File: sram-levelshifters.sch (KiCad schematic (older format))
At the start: 5 parts, among them U1 74HC04, U7 ISSI61WV5128BL, U8 ISSI61WV5128BL

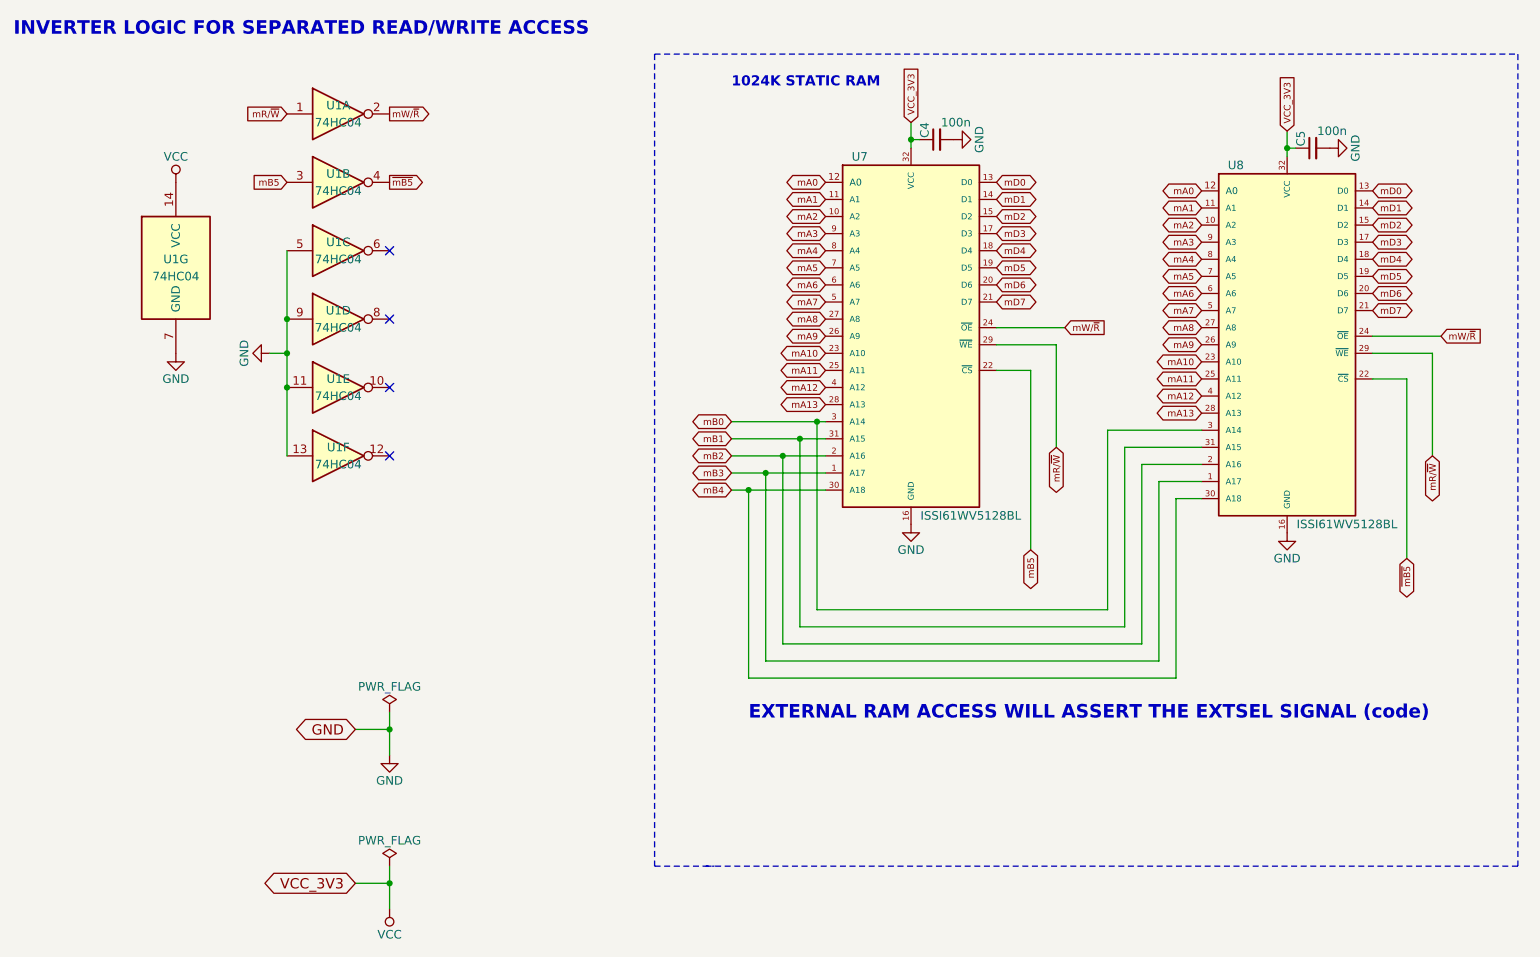
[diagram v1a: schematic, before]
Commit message: Upgraded to a dual chip select for external SRAM. In this case up to 1536k can be addressable
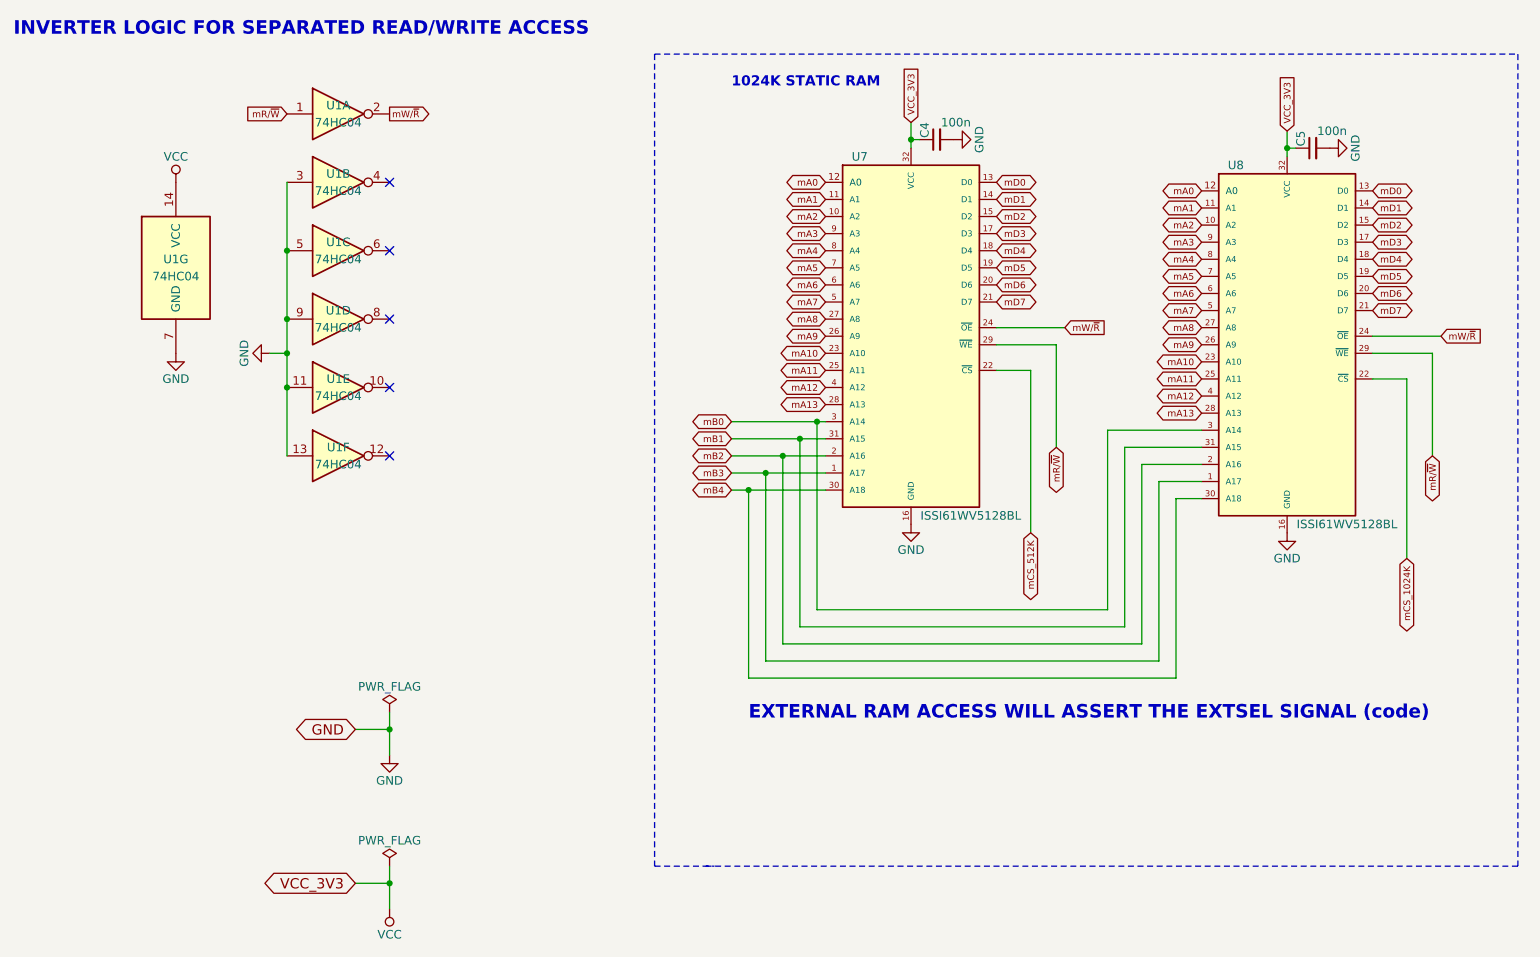
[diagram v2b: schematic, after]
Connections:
- net GND: now also U1.3
- net mB5 renamed mCS_512K
- net mCS_512K: no longer U1.3
- net ~mB5: no longer names the net of U1.4
- net ~mB5: no longer U8.22 (~CS)
- new net mCS_1024K: U8.22 (~CS)
- no-connect marks 4 -> 5
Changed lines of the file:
@@
 Wire Wire Line
 	7050 3300 7250 3300
-Wire Wire Line
-	7250 3300 7250 4350
-Text GLabel 7250 4350 3    39   BiDi ~ 0
-mB5
+Text GLabel 7250 4250 3    39   BiDi ~ 0
+mCS_512K
 Text Notes 5600 5350 0    79   ~ 16
 EXTERNAL RAM ACCESS WILL ASSERT THE EXTSEL SIGNAL (code)
@@
 Wire Wire Line
 	9450 3350 9450 4400
-Text GLabel 9450 4400 3    39   BiDi ~ 0
-~mB5
 Wire Wire Line
 	5500 3600 6050 3600
@@
 	1    0    0    -1
 $EndComp
-Text GLabel 2900 2200 0    39   Input ~ 0
-mB5
-Text GLabel 3500 2200 2    39   Output ~ 0
-~mB5
 Text Notes 1300 1350 0    79   ~ 16
 INVERTER LOGIC FOR SEPARATED READ/WRITE ACCESS
@@
 $EndComp
 Wire Wire Line
-	2900 2600 2900 3800
+	2900 2200 2900 3800
 Connection ~ 2900 3000
 Connection ~ 2900 3400
@@
 	2800 3200 2900 3200
 Connection ~ 2900 3200
+Connection ~ 2900 2600
+NoConn ~ 3500 2200
+Wire Wire Line
+	7250 3300 7250 4250
+Text GLabel 9450 4400 3    39   BiDi ~ 0
+mCS_1024K
 $EndSCHEMATC

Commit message: Added nOE and nWE from the GPIOs
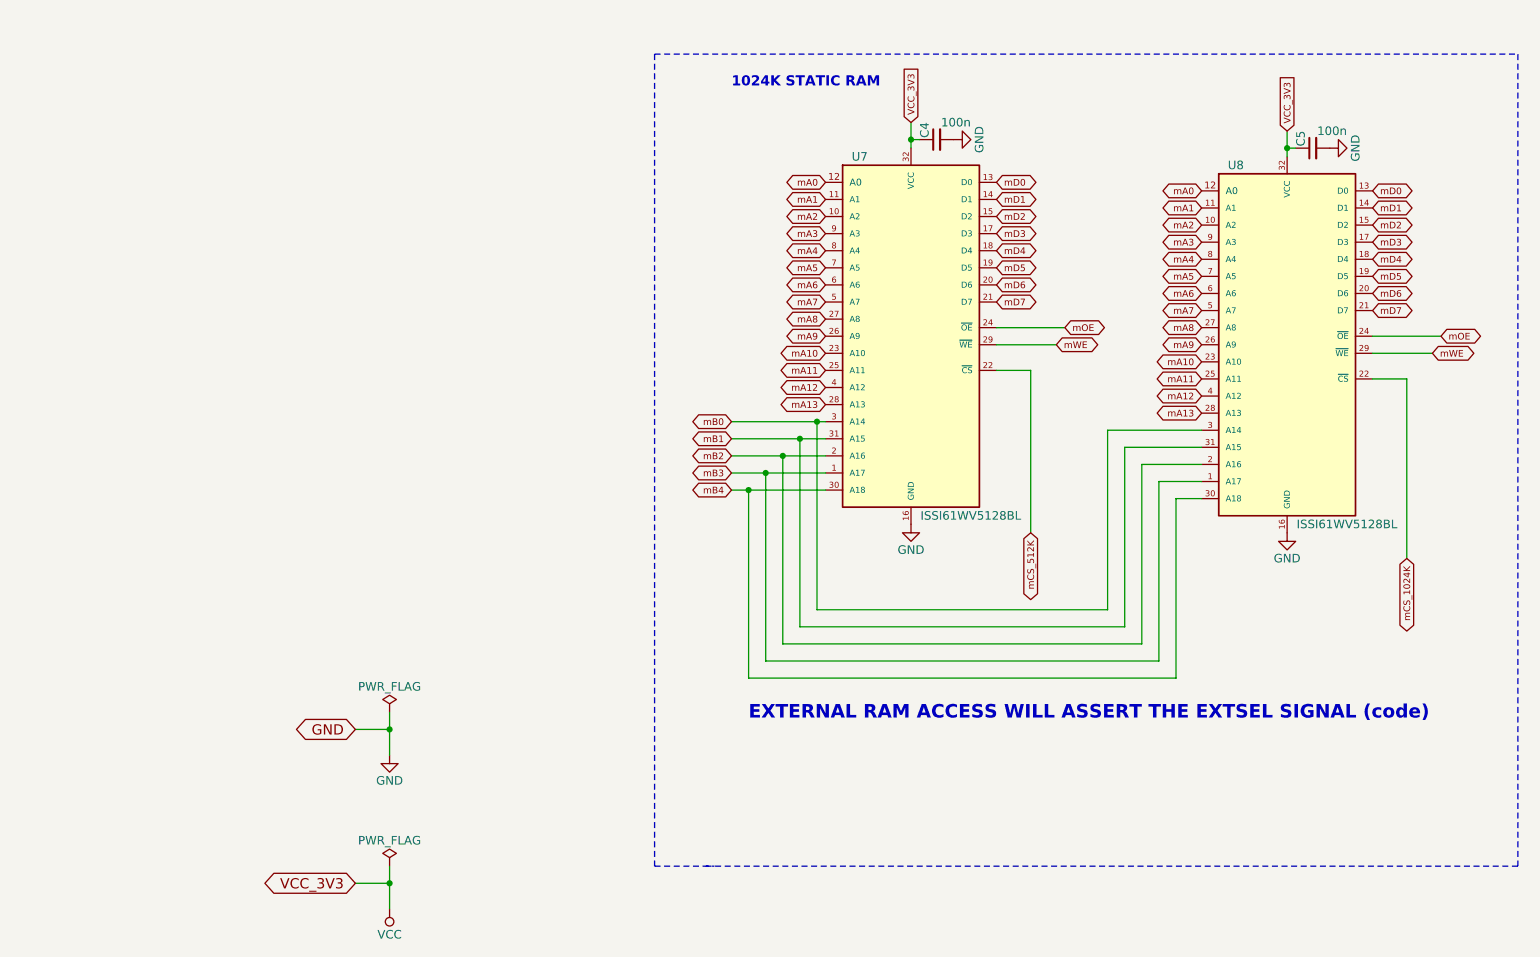
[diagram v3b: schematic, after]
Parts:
- removed U1: 74HC04, RetroBitLab:PSOP14-5x7.40-1.27, symbol 74HC04
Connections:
- net mR/~W renamed mWE
- net mW/~R renamed mOE
- no-connect marks 5 -> 0
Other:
- note removed: "INVERTER LOGIC FOR SEPARATED READ/WRITE ACCESS"
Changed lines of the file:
@@
 Text GLabel 6550 1850 1    39   Input ~ 0
 VCC_3V3
-Text GLabel 7400 3750 3    39   BiDi ~ 0
-mR/~W
 Wire Wire Line
 	7050 3150 7400 3150
-Wire Wire Line
-	7400 3150 7400 3750
 Wire Wire Line
 	6550 1850 6550 2000
@@
 Text GLabel 8750 1900 1    39   Input ~ 0
 VCC_3V3
-Text GLabel 9600 3800 3    39   BiDi ~ 0
-mR/~W
 Wire Wire Line
 	9250 3200 9600 3200
-Wire Wire Line
-	9600 3200 9600 3800
 Wire Wire Line
 	8750 1900 8750 2050
@@
 Wire Wire Line
 	7450 3050 7050 3050
-$Comp
-L 74HC04 U1
-U 1 1 5CC43BF6
-P 3200 1800
-F 0 "U1" H 3200 1850 50  0000 C CNN
-F 1 "74HC04" H 3200 1750 50  0000 C CNN
-F 2 "RetroBitLab:PSOP14-5x7.40-1.27" H 3200 1800 50  0001 C CNN
-F 3 "" H 3200 1800 50  0001 C CNN
-	1    3200 1800
-	1    0    0    -1
-$EndComp
-Text GLabel 2900 1800 0    39   Input ~ 0
-mR/~W
-Text GLabel 3500 1800 2    39   Output ~ 0
-mW/~R
-Text GLabel 7450 3050 2    39   Input ~ 0
-mW/~R
-Text GLabel 9650 3100 2    39   Input ~ 0
-mW/~R
-$Comp
-L 74HC04 U1
-U 2 1 5CC43DF2
-P 3200 2200
-F 0 "U1" H 3200 2250 50  0000 C CNN
-F 1 "74HC04" H 3200 2150 50  0000 C CNN
-F 2 "RetroBitLab:PSOP14-5x7.40-1.27" H 3200 2200 50  0001 C CNN
-F 3 "" H 3200 2200 50  0001 C CNN
-	2    3200 2200
-	1    0    0    -1
-$EndComp
-Text Notes 1300 1350 0    79   ~ 16
-INVERTER LOGIC FOR SEPARATED READ/WRITE ACCESS
-$Comp
-L 74HC04 U1
-U 3 1 5CC43E84
-P 3200 2600
-F 0 "U1" H 3200 2650 50  0000 C CNN
-F 1 "74HC04" H 3200 2550 50  0000 C CNN
-F 2 "RetroBitLab:PSOP14-5x7.40-1.27" H 3200 2600 50  0001 C CNN
-F 3 "" H 3200 2600 50  0001 C CNN
-	3    3200 2600
-	1    0    0    -1
-$EndComp
-$Comp
-L 74HC04 U1
-U 4 1 5CC43EC9
-P 3200 3000
-F 0 "U1" H 3200 3050 50  0000 C CNN
-F 1 "74HC04" H 3200 2950 50  0000 C CNN
-F 2 "RetroBitLab:PSOP14-5x7.40-1.27" H 3200 3000 50  0001 C CNN
-F 3 "" H 3200 3000 50  0001 C CNN
-	4    3200 3000
-	1    0    0    -1
-$EndComp
-$Comp
-L 74HC04 U1
-U 5 1 5CC43F00
-P 3200 3400
-F 0 "U1" H 3200 3450 50  0000 C CNN
-F 1 "74HC04" H 3200 3350 50  0000 C CNN
-F 2 "RetroBitLab:PSOP14-5x7.40-1.27" H 3200 3400 50  0001 C CNN
-F 3 "" H 3200 3400 50  0001 C CNN
-	5    3200 3400
-	1    0    0    -1
-$EndComp
-$Comp
-L 74HC04 U1
-U 6 1 5CC43FFF
-P 3200 3800
-F 0 "U1" H 3200 3850 50  0000 C CNN
-F 1 "74HC04" H 3200 3750 50  0000 C CNN
-F 2 "RetroBitLab:PSOP14-5x7.40-1.27" H 3200 3800 50  0001 C CNN
-F 3 "" H 3200 3800 50  0001 C CNN
-	6    3200 3800
-	1    0    0    -1
-$EndComp
-$Comp
-L 74HC04 U1
-U 7 1 5CC4404C
-P 2250 2700
-F 0 "U1" H 2250 2750 50  0000 C CNN
-F 1 "74HC04" H 2250 2650 50  0000 C CNN
-F 2 "RetroBitLab:PSOP14-5x7.40-1.27" H 2250 2700 50  0001 C CNN
-F 3 "" H 2250 2700 50  0001 C CNN
-	7    2250 2700
-	1    0    0    -1
-$EndComp
-$Comp
-L GND #PWR017
-U 1 1 5CC440E8
-P 2250 3200
-F 0 "#PWR017" H 2250 2950 50  0001 C CNN
-F 1 "GND" H 2250 3050 50  0000 C CNN
-F 2 "" H 2250 3200 50  0001 C CNN
-F 3 "" H 2250 3200 50  0001 C CNN
-	1    2250 3200
-	1    0    0    -1
-$EndComp
-$Comp
-L VCC #PWR018
-U 1 1 5CC44114
-P 2250 2200
-F 0 "#PWR018" H 2250 2050 50  0001 C CNN
-F 1 "VCC" H 2250 2350 50  0000 C CNN
-F 2 "" H 2250 2200 50  0001 C CNN
-F 3 "" H 2250 2200 50  0001 C CNN
-	1    2250 2200
-	1    0    0    -1
-$EndComp
-Wire Wire Line
-	2900 2200 2900 3800
-Connection ~ 2900 3000
-Connection ~ 2900 3400
-NoConn ~ 3500 2600
-NoConn ~ 3500 3000
-NoConn ~ 3500 3400
-NoConn ~ 3500 3800
-$Comp
-L GND #PWR019
-U 1 1 5CC44296
-P 2800 3200
-F 0 "#PWR019" H 2800 2950 50  0001 C CNN
-F 1 "GND" H 2800 3050 50  0000 C CNN
-F 2 "" H 2800 3200 50  0001 C CNN
-F 3 "" H 2800 3200 50  0001 C CNN
-	1    2800 3200
-	0    1    1    0
-$EndComp
-Wire Wire Line
-	2800 3200 2900 3200
-Connection ~ 2900 3200
-Connection ~ 2900 2600
-NoConn ~ 3500 2200
 Wire Wire Line
 	7250 3300 7250 4250
 Text GLabel 9450 4400 3    39   BiDi ~ 0
 mCS_1024K
+Text GLabel 9650 3100 2    39   BiDi ~ 0
+mOE
+Text GLabel 9600 3200 2    39   BiDi ~ 0
+mWE
+Text GLabel 7450 3050 2    39   BiDi ~ 0
+mOE
+Text GLabel 7400 3150 2    39   BiDi ~ 0
+mWE
 $EndSCHEMATC

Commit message: New layout and design
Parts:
- removed C5: 100n, Capacitors_SMD:C_1206_HandSoldering, symbol C_Small
- removed U8: ISSI61WV5128BL, RetroBitLab:SOP-32L-20.5x11.30-1.27mm, symbol ISSI61WV5128BL
- added C3: 100n, Capacitors_SMD:C_1206_HandSoldering, symbol C_Small
- added U2: ISSI61WV5128BL, RetroBitLab:SOP-32L-20.5x11.30-1.27mm, symbol ISSI61WV5128BL
- renumbered C4 to C2, U7 to U1
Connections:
- net GND: now also C3.2, U2.16 (GND)
- net VCC: now also C3.1, U2.32 (VCC)
- net mA0 renamed FSMC_A0
- net FSMC_A0: now also U2.12 (A0)
- net mA1 renamed FSMC_A1
- net FSMC_A1: now also U2.11 (A1)
- net mA10 renamed FSMC_A10
- net FSMC_A10: now also U2.23 (A10)
- net mA11 renamed FSMC_A11
- net FSMC_A11: now also U2.25 (A11)
- net mA12 renamed FSMC_A12
- net FSMC_A12: now also U2.4 (A12)
- net mA13 renamed FSMC_A13
- net FSMC_A13: now also U2.28 (A13)
- net mA2 renamed FSMC_A2
- net FSMC_A2: now also U2.10 (A2)
- net mA3 renamed FSMC_A3
- net FSMC_A3: now also U2.9 (A3)
- net mA4 renamed FSMC_A4
- net FSMC_A4: now also U2.8 (A4)
- net mA5 renamed FSMC_A5
- net FSMC_A5: now also U2.7 (A5)
- net mA6 renamed FSMC_A6
- net FSMC_A6: now also U2.6 (A6)
- net mA7 renamed FSMC_A7
- net FSMC_A7: now also U2.5 (A7)
- net mA8 renamed FSMC_A8
- net FSMC_A8: now also U2.27 (A8)
- net mA9 renamed FSMC_A9
- net FSMC_A9: now also U2.26 (A9)
- net mB0 renamed FSMC_A14
- net FSMC_A14: now also U2.3 (A14)
- net mB1 renamed FSMC_A15
- net FSMC_A15: now also U2.31 (A15)
- net mB2 renamed FSMC_A16
- net FSMC_A16: now also U2.2 (A16)
- net mB3 renamed FSMC_A17
- net FSMC_A17: now also U2.1 (A17)
- net mB4 renamed FSMC_A18
- net FSMC_A18: now also U2.30 (A18)
- net mCS_512K renamed FSMC_NE1
- net mD0 renamed FSMC_D0
- net FSMC_D0: now also U2.13 (D0)
- net mD1 renamed FSMC_D1
- net FSMC_D1: now also U2.14 (D1)
- net mD2 renamed FSMC_D2
- net FSMC_D2: now also U2.15 (D2)
- net mD3 renamed FSMC_D3
- net FSMC_D3: now also U2.17 (D3)
- net mD4 renamed FSMC_D4
- net FSMC_D4: now also U2.18 (D4)
- net mD5 renamed FSMC_D5
- net FSMC_D5: now also U2.19 (D5)
- net mD6 renamed FSMC_D6
- net FSMC_D6: now also U2.20 (D6)
- net mD7 renamed FSMC_D7
- net FSMC_D7: now also U2.21 (D7)
- net mOE renamed FSMC_NOE
- net FSMC_NOE: now also U2.24 (~OE)
- net mWE renamed FSMC_NWE
- net FSMC_NWE: now also U2.29 (~WE)
- new net FSMC_NE2: U2.22 (~CS)
